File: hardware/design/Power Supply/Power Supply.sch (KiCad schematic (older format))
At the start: 26 parts

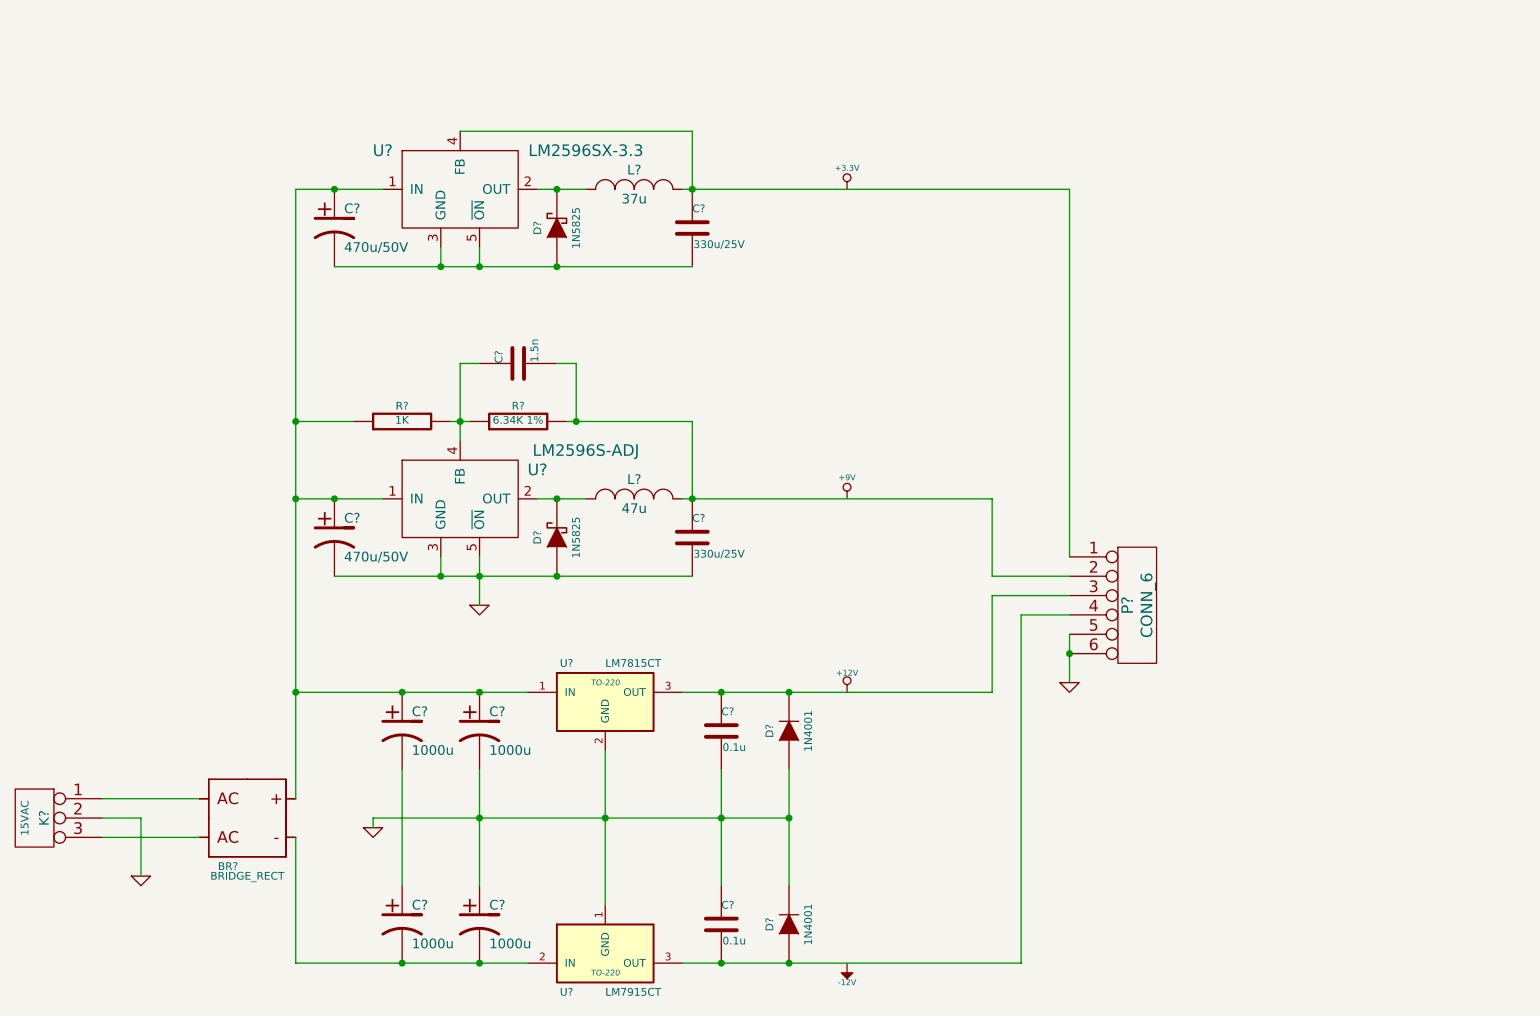
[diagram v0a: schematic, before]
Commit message: Power Supply Design
First Pass at Power Supply PCB design
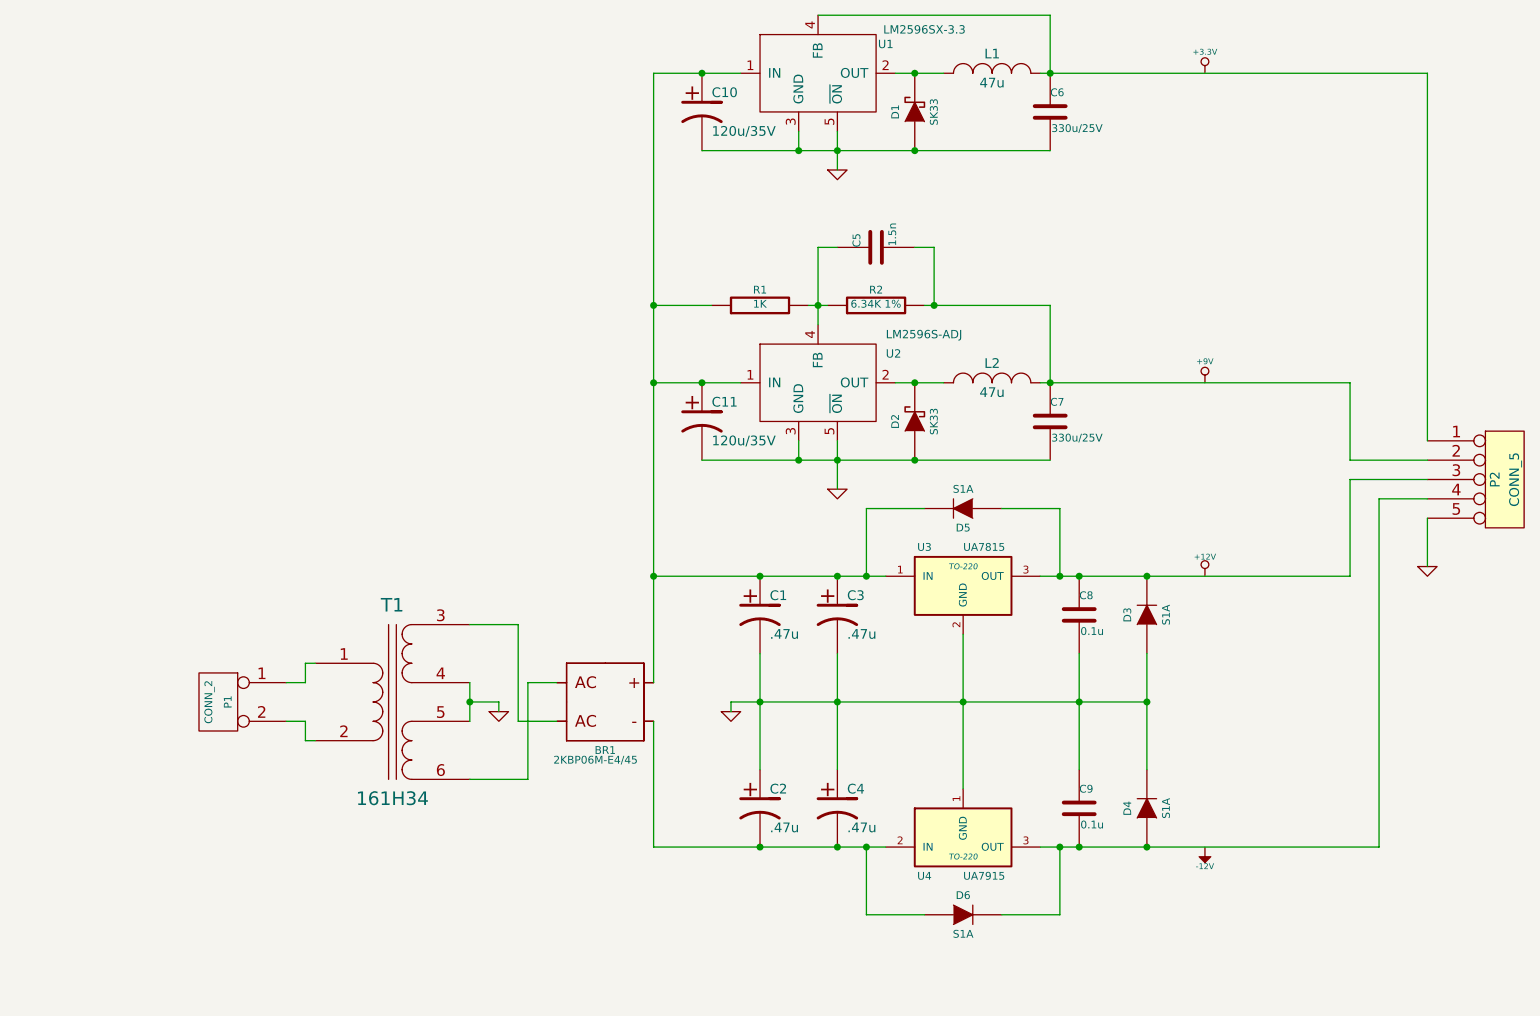
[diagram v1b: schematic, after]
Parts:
- removed BR?: BRIDGE_RECT, ~, symbol BRIDGE_RECT
- removed C? (x2): 470u/50V, ~, symbol CP1
- removed K?: 15VAC, symbol CONN_3
- removed P?: CONN_6, symbol CONN_6
- added BR1: 2KBP06M-E4/45, ~, symbol BRIDGE_RECT
- added C10, C11: 120u/35V, ~, symbol CP1
- added D5, D6: S1A, ~, symbol DIODE
- added P1: CONN_2, symbol CONN_2
- added P2: CONN_5, symbol CONN_5
- added T1: 161H34, ~, symbol TRANSFO2
- C1, C2, C3, C4: renamed from C?; value 1000u -> .47u
- D1, D2: renamed from D?; value 1N5825 -> SK33
- D3, D4: renamed from D?; value 1N4001 -> S1A
- L1: renamed from L?; value 37u -> 47u
- U3: renamed from U?; value LM7815CT -> UA7815
- U4: renamed from U?; value LM7915CT -> UA7915
- gave numbers to parts that had none: 10
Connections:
- net GND: now also C1.2, C2.1, C6.2, D1.1 (A), U1.3 (GND), U1.5 (~ON), C10.2, C11.2, P2.5, T1.4 (SB), T1.5 (SC)
- net at C1.1, C3.1, R1.1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: now also BR1.1 (POS), C10.1, C11.1, D5.2 (K)
- net at C2.2, C4.2, U4.2 (IN): now also BR1.4 (NEG), D6.1 (A)
- net at C8.1, D3.2 (K), U3.3 (OUT): now also D5.1 (A), P2.3
- net at C9.2, D4.1 (A), U4.3 (OUT): now also D6.2 (K), P2.4
- net at C5.2, C7.1, L2.2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: now also P2.2
- net at C6.1, L1.2, U1.4 (FB): now also P2.1
- new net: P1.1 (P1), T1.1 (AA)
- new net: P1.2 (PM), T1.2 (AB)
- new net: BR1.3 (AC_IN), T1.3 (SA)
- new net: BR1.2 (AC_IN), T1.6 (SD)
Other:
- moved on the sheet: C1, C2, C3, C4, C5, C6, C7, C8, C9, D1, D2, D3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

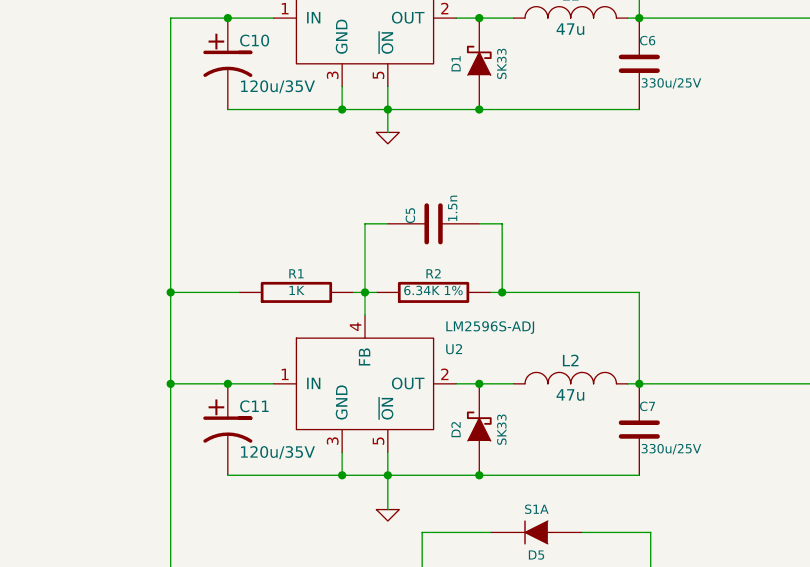
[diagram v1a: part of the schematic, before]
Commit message: Power Supply Design
Working update. Changing 9V rail to 5V.
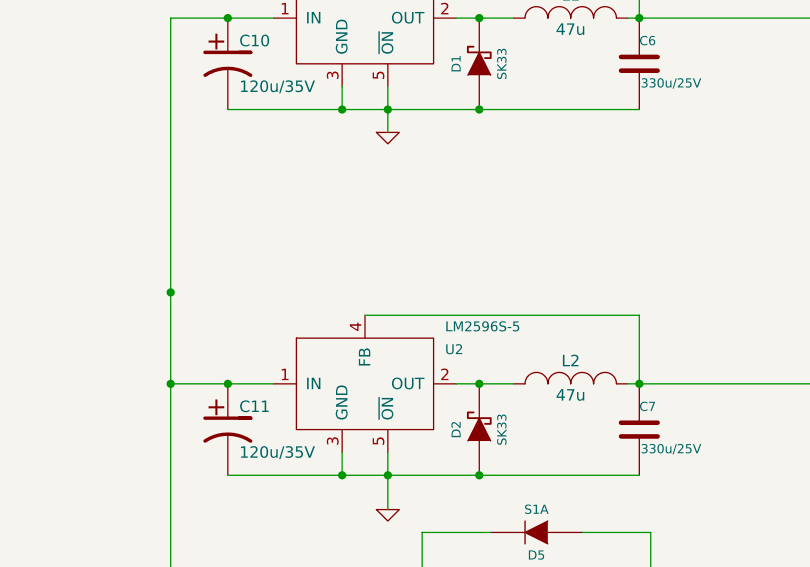
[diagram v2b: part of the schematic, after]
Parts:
- removed C5: 1.5n, ~, symbol C
- removed R1: 1K, ~, symbol R
- removed R2: 6.34K 1%, ~, symbol R
- U2: value LM2596S-ADJ -> LM2596S-5
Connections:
- net at U2.4 (FB): now also C7.1, L2.2, P2.2
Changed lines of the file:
@@
 LIBS:contrib
 LIBS:valves
-LIBS:P14345
 LIBS:Power Supply-cache
 EELAYER 27 0
@@
 P 5750 3250
 F 0 "U2" H 6100 3400 43  0000 L CNN
-F 1 "LM2596S-ADJ" H 6100 3500 43  0000 L CNN
+F 1 "LM2596S-5" H 6100 3500 43  0000 L CNN
 F 2 "" H 5750 3250 60  0000 C CNN
 F 3 "" H 5750 3250 60  0000 C CNN
 	1    5750 3250
 	1    0    0    -1
-$EndComp
-$Comp
-L R R1
-U 1 1 534183F0
-P 5450 2850
-F 0 "R1" V 5530 2850 40  0000 C CNN
-F 1 "1K" V 5457 2851 40  0000 C CNN
-F 2 "~" V 5380 2850 30  0000 C CNN
-F 3 "~" H 5450 2850 30  0000 C CNN
-	1    5450 2850
-	0    -1   -1   0
-$EndComp
-$Comp
-L R R2
-U 1 1 5341841D
-P 6050 2850
-F 0 "R2" V 6130 2850 40  0000 C CNN
-F 1 "6.34K 1%" V 6057 2851 40  0000 C CNN
-F 2 "~" V 5980 2850 30  0000 C CNN
-F 3 "~" H 6050 2850 30  0000 C CNN
-	1    6050 2850
-	0    -1   -1   0
 $EndComp
 $Comp
@@
 $EndComp
 $Comp
-L C C5
-U 1 1 534187A0
-P 6050 2550
-F 0 "C5" H 6050 2650 40  0000 L CNN
-F 1 "1.5n" H 6056 2465 40  0000 L CNN
-F 2 "~" H 6088 2400 30  0000 C CNN
-F 3 "~" H 6050 2550 60  0000 C CNN
-	1    6050 2550
-	0    -1   -1   0
-$EndComp
-$Comp
 L GND #PWR03
 U 1 1 5341FA37
@@
 Connection ~ 4900 2850
 Connection ~ 5650 3650
-Connection ~ 6350 2850
-Wire Wire Line
-	6350 2550 6350 2850
-Wire Wire Line
-	6250 2550 6350 2550
-Wire Wire Line
-	5750 2550 5850 2550
-Wire Wire Line
-	6950 2850 6950 3250
-Wire Wire Line
-	6300 2850 6950 2850
 Wire Wire Line
 	6900 3250 8500 3250
@@
 Wire Wire Line
 	5650 3650 5650 3550
-Wire Wire Line
-	5200 2850 4900 2850
-Connection ~ 5750 2850
-Wire Wire Line
-	5750 2550 5750 2950
-Wire Wire Line
-	5800 2850 5700 2850
 Connection ~ 4900 4250
 Connection ~ 7450 4900
@@
 Wire Wire Line
 	4200 5000 4400 5000
+Wire Wire Line
+	5750 2950 6950 2950
+Wire Wire Line
+	6950 2950 6950 3250
 $EndSCHEMATC
